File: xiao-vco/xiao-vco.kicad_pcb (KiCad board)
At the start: 2 copper layers, 38 x 100 mm, 67 parts, among them J1 C2M, J2 C2F, J3 Eurorack Power, J4 CV1, J5 V/OCT, J6 OUT, J7 CV2, J8 C1M, J9 C1F, U1 SeeeduinoXIAO, U2 MCP6002-xSN, U3 MCP6002-xSN, U4 TL072, U5 LM1117-5.0, U6 LM4040DBZ-10

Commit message: Update text
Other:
- board text added: "Nostrum Rev. 1 Paul Battley 2022 CC-BY-SA-4.0"
- board text added: "← Output range with: ±8V without: ±5V"
- board text removed: "JOAT Rev. 1 Paul Battley 2022 CC-BY-SA-4.0"
- board text removed: "← With: ±8V Without: ±5V"
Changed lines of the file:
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@@
     (effects (font (size 1 1) (thickness 0.1524)) (justify mirror))
   )
-  (gr_text "← With: ±8V\nWithout: ±5V" (at 173.114 67.145) (layer "B.SilkS")
+  (gr_text "← Output range\nwith: ±8V\nwithout: ±5V" (at 171.59 66.637) (layer "B.SilkS")
     (effects (font (size 1 1) (thickness 0.1524)) (justify right mirror))
   )
@@
     (effects (font (size 1 1) (thickness 0.1524)) (justify left mirror))
   )
-  (gr_text "JOAT Rev. 1\nPaul Battley 2022\nCC-BY-SA-4.0" (at 179.5656 53.7338) (layer "B.SilkS")
+  (gr_text "Nostrum Rev. 1\nPaul Battley 2022\nCC-BY-SA-4.0" (at 179.5656 53.7338) (layer "B.SilkS")
     (effects (font (size 1 1) (thickness 0.1524)) (justify mirror))
   )

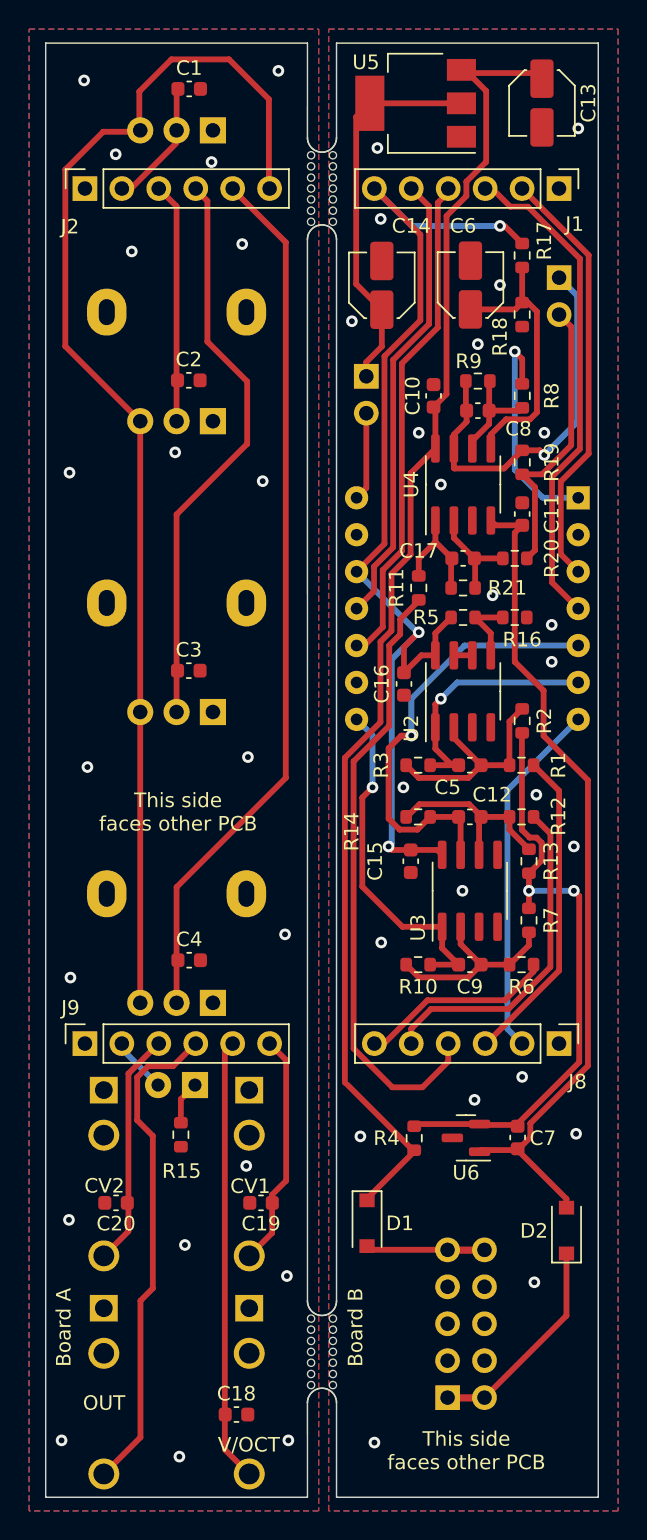
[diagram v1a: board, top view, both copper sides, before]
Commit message: Tweak layout, fix CV gain
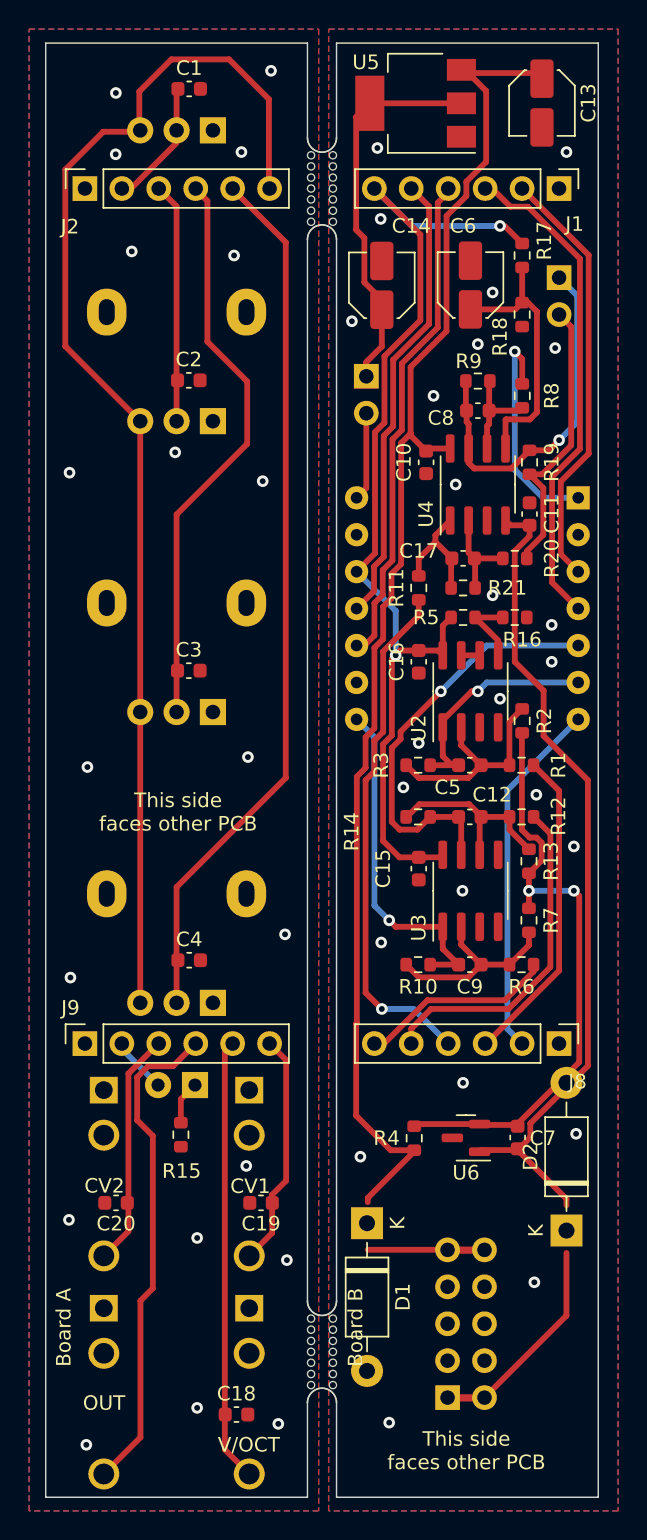
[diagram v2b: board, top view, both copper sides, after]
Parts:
- D1, D2: footprint Personal:SOD-123FL -> Diode_THT:D_DO-41_SOD81_P10.16mm_Horizontal
- R10, R3: value 100k -> 33k
- moved C10 4.60 mm to (176.2, 78.8), turned to -90 degrees
- moved C16 1.83 mm to (175.7, 92.5)
- moved U4 1.01 mm to (179.7, 80.4)
- moved C15 0.75 mm to (175.7, 106.8)
- moved U2 0.51 mm to (179.2, 94.6)
- moved C11 0.51 mm to (183.3, 82.4)
- moved R19 0.51 mm to (183.3, 78.8)
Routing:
- net /JACK_OUT: track 42.2 -> 35.6 mm, vias 0 -> 1
- net +12V: track 91.0 -> 94.7 mm
- net +3V3: track 75.6 -> 72.2 mm, vias 3 -> 2
- net Net-(C8-Pad1): track 26.9 -> 25.1 mm
- net /VOCT_IN: track 30.5 -> 29.0 mm
- net /CV2_IN: track 17.1 -> 15.7 mm
- net GND: vias 23 -> 24
